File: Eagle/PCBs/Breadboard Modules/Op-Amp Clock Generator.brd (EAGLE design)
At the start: 17.8 x 38.1 mm, 20 parts, among them Q1 2N7002, Q2 2N7002, U1 TL072P

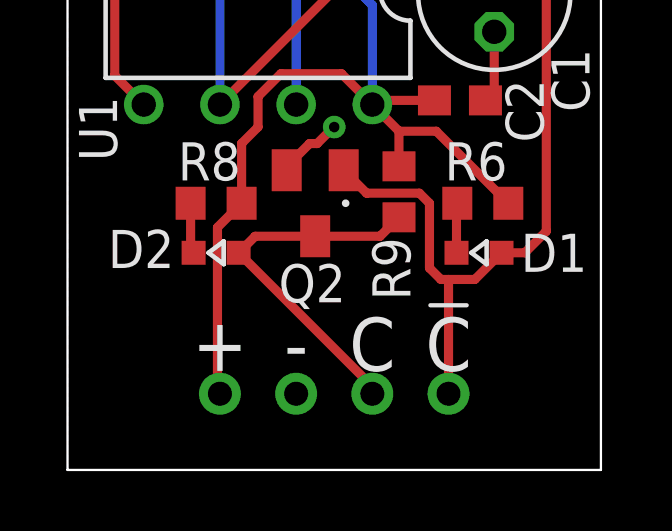
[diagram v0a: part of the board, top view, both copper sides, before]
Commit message: Update Op-Amp Clock Generator.brd
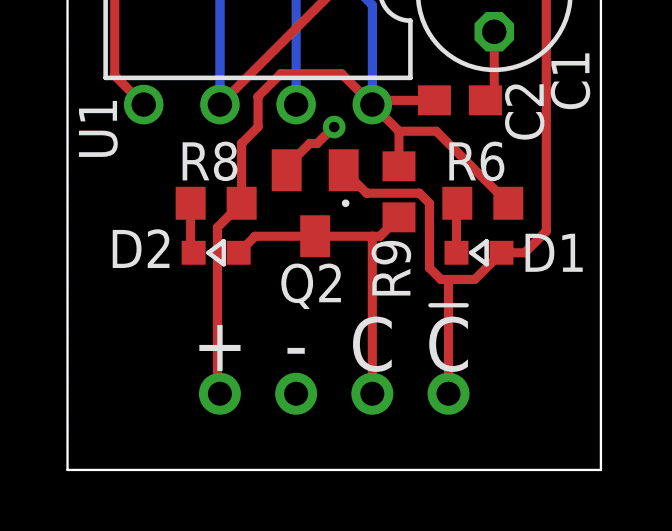
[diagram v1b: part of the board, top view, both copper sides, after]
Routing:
- net CLK: track 12.4 -> 11.1 mm
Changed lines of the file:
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@@
 </layers>
 <board>
+<fusionsync huburn="a.cGVyc29uYWw6dWUyZGY0M2Ex" projecturn="a.cGVyc29uYWw6dWUyZGY0M2ExIzIwMjMwNDIzNjMzMDQzOTMx" f3durn="urn:adsk.wipprod:dm.lineage:43MyuvAlQZ68AYFzXby8wg" pcbguid="1708b203-b104-45be-8383-4d59b23a664c" lastpulledtime="" lastsyncedchangeguid="" latestrevisionid="f2156ed4-a625-4df9-8ccf-9667e721271c" lastsyncedrevisionid="f2156ed4-a625-4df9-8ccf-9667e721271c" lastboardhashguid="c2ab819f-2bf1-c68c-863e-b8a479f81b6d" lastpushedtime="2023-05-12T08:22:23Z" linktopcb3d="true"/>
 <plain>
 <wire x1="0" y1="0" x2="0" y2="38.1" width="0.0762" layer="20"/>
@@
 <contactref element="R9" pad="1"/>
 <contactref element="D2" pad="A"/>
-<wire x1="8.255" y1="7.79" x2="10.418" y2="7.79" width="0.3048" layer="1"/>
+<wire x1="8.255" y1="7.79" x2="10.16" y2="7.79" width="0.3048" layer="1"/>
+<wire x1="10.16" y1="7.79" x2="10.418" y2="7.79" width="0.3048" layer="1"/>
 <wire x1="10.418" y1="7.79" x2="11.049" y2="8.421" width="0.3048" layer="1"/>
 <wire x1="5.703" y1="7.239" x2="6.254" y2="7.79" width="0.3048" layer="1"/>
 <wire x1="6.254" y1="7.79" x2="8.255" y2="7.79" width="0.3048" layer="1"/>
 <contactref element="CLK" pad="P1"/>
-<wire x1="5.703" y1="7.239" x2="10.16" y2="2.782" width="0.3048" layer="1"/>
-<wire x1="10.16" y1="2.782" x2="10.16" y2="2.54" width="0.3048" layer="1"/>
+<wire x1="10.16" y1="2.54" x2="10.16" y2="7.79" width="0.3048" layer="1"/>
 </signal>
 </signals>
@@
 </note>
 <note version="8.3" severity="warning">
+Since Version 8.3, EAGLE supports Fusion synchronisation.
+This feature will not be available in this version and saving
+the document will break the link to the Fusion PCB feature.
+</note>
+<note version="8.3" severity="warning">
